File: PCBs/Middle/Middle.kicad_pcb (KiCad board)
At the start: 2 copper layers, 82 x 82 mm, 0 parts

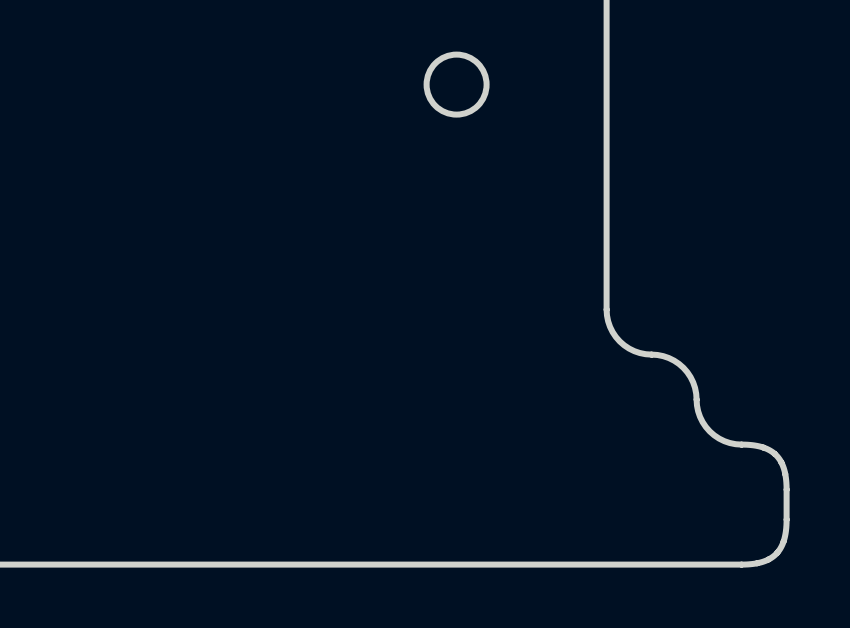
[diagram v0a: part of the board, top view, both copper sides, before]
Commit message: USB-C contact added to mid
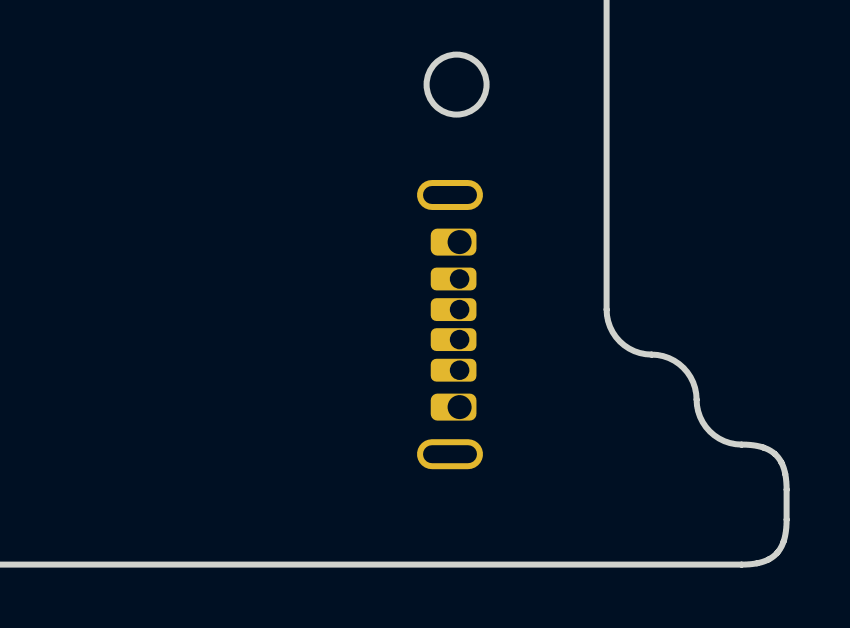
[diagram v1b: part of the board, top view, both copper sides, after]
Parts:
- added J1: USB_C_Receptacle_PowerOnly_6P, Library:TYPE-C-31-D-08, B.Cu at (158.4, 134.0)
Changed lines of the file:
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@@
   )
   (net 0 "")
+  (net 1 "/CC1")
+  (net 2 "+5V")
+  (net 3 "GND")
+  (net 4 "/CC2")
+  (footprint "Library:TYPE-C-31-D-08" (layer "B.Cu")
+    (at 158.45 134 90)
+    (property "Sheetfile" "Middle.kicad_sch")
+    (property "Sheetname" "")
+    (property "ki_description" "USB Power-Only 6P Type-C Receptacle connector")
+    (property "ki_keywords" "usb universal serial bus type-C power-only charging-only 6P 6C")
+    (attr through_hole)
+    (fp_text reference "J1" (at -0.1 4.75 270 unlocked) (layer "B.SilkS")
+        (effects (font (size 1 1) (thickness 0.15)) (justify mirror))
+    )
+    (fp_text value "USB_C_Receptacle_PowerOnly_6P" (at -0.1 -1.45 270 unlocked) (layer "B.Fab")
+        (effects (font (size 1 1) (thickness 0.15)) (justify mirror))
+    )
+    (fp_text user "${REFERENCE}" (at -0.2 -2.95 270 unlocked) (layer "B.Fab")
+        (effects (font (size 1 1) (thickness 0.15)) (justify mirror))
+    )
+    (fp_line (start -4.47 1.3) (end -4.47 1.86)
+      (stroke (width 0.1) (type default)) (layer "B.SilkS"))
+    (fp_line (start -3.17 3.16) (end 3.17 3.16)
+      (stroke (width 0.1) (type default)) (layer "B.SilkS"))
+    (fp_line (start 3.17 0) (end -3.17 0)
+      (stroke (width 0.1) (type default)) (layer "B.SilkS"))
+    (fp_line (start 4.47 1.86) (end 4.47 1.3)
+      (stroke (width 0.1) (type default)) (layer "B.SilkS"))
+    (fp_arc (start -4.47 1.3) (mid -4.089239 0.380761) (end -3.17 0)
+      (stroke (width 0.1) (type default)) (layer "B.SilkS"))
+    (fp_arc (start -3.17 3.16) (mid -4.089239 2.779239) (end -4.47 1.86)
+      (stroke (width 0.1) (type default)) (layer "B.SilkS"))
+    (fp_arc (start 3.17 0) (mid 4.089239 0.380761) (end 4.47 1.3)
+      (stroke (width 0.1) (type default)) (layer "B.SilkS"))
+    (fp_arc (start 4.47 1.86) (mid 4.089239 2.779239) (end 3.17 3.16)
+      (stroke (width 0.1) (type default)) (layer "B.SilkS"))
+    (pad "A5" thru_hole roundrect (at -0.5 1.65 90) (size 0.762 1.524) (drill 0.65 (offset 0 -0.2)) (layers "*.Cu" "*.Mask") (roundrect_rratio 0.25)
+      (net 1 "/CC1") (pinfunction "CC1") (pintype "bidirectional"))
+    (pad "A9" thru_hole roundrect (at 1.52 1.65 90) (size 0.762 1.524) (drill 0.65 (offset 0 -0.2)) (layers "*.Cu" "*.Mask") (roundrect_rratio 0.25)
+      (net 2 "+5V") (pinfunction "VBUS") (pintype "passive"))
+    (pad "A12" thru_hole roundrect (at 2.75 1.65 90) (size 0.9 1.524) (drill 0.8 (offset 0 -0.2)) (layers "*.Cu" "*.Mask") (roundrect_rratio 0.25)
+      (net 3 "GND") (pinfunction "GND") (pintype "passive"))
+    (pad "B5" thru_hole roundrect (at 0.5 1.65 90) (size 0.762 1.524) (drill 0.65 (offset 0 -0.2)) (layers "*.Cu" "*.Mask") (roundrect_rratio 0.25)
+      (net 4 "/CC2") (pinfunction "CC2") (pintype "bidirectional"))
+    (pad "B9" thru_hole roundrect (at -1.52 1.65 90) (size 0.762 1.524) (drill 0.65 (offset 0 -0.2)) (layers "*.Cu" "*.Mask") (roundrect_rratio 0.25)
+      (net 2 "+5V") (pinfunction "VBUS") (pintype "passive"))
+    (pad "B12" thru_hole roundrect (at -2.75 1.65 90) (size 0.9 1.524) (drill 0.8 (offset 0 -0.2)) (layers "*.Cu" "*.Mask") (roundrect_rratio 0.25)
+      (net 3 "GND") (pinfunction "GND") (pintype "passive"))
+    (pad "S1" thru_hole oval (at -4.32 1.33 90) (size 1 2.2) (drill oval 0.6 1.8) (layers "*.Cu" "*.Mask")
+      (net 3 "GND") (pinfunction "SHIELD") (pintype "passive"))
+    (pad "S1" thru_hole oval (at 4.32 1.33 90) (size 1 2.2) (drill oval 0.6 1.8) (layers "*.Cu" "*.Mask")
+      (net 3 "GND") (pinfunction "SHIELD") (pintype "passive"))
+    (model "${KIPRJMOD}/Library.pretty/footprint_test-v2.step"
+      (offset (xyz -15.8 -5.56 0))
+      (scale (xyz 1 1 1))
+      (rotate (xyz -90 0 -90))
+    )
+  )
   (gr_line locked (start 161.7 131.1) (end 161.7 136.9)
     (stroke (width 0.2) (type solid)) (layer "Cmts.User"))

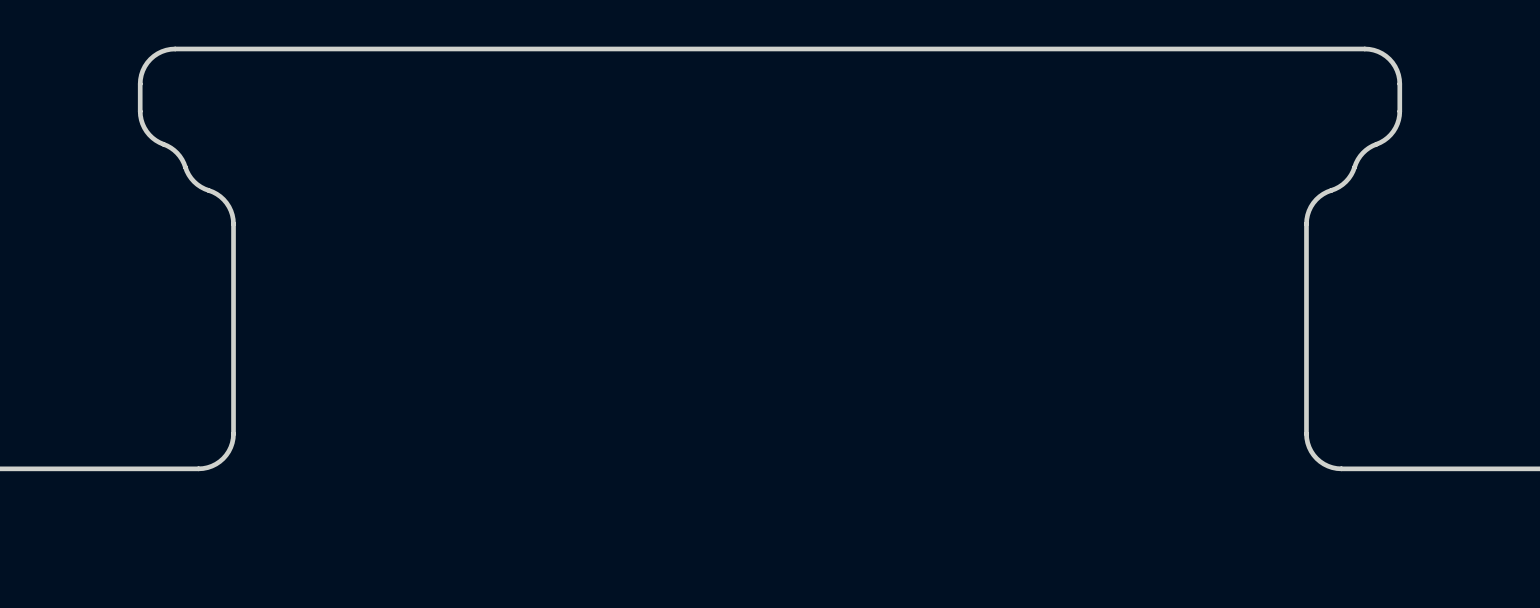
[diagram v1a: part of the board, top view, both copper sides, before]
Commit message: Middle silks
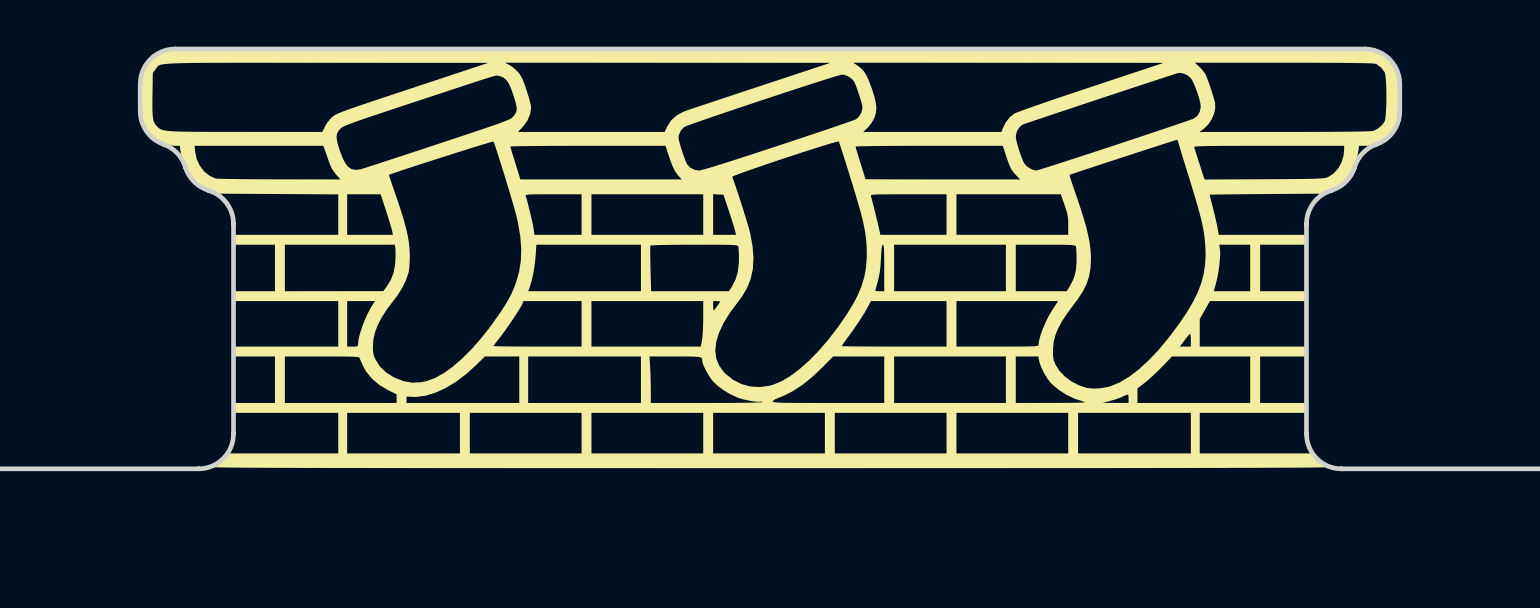
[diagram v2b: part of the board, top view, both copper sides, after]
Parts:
- added G***: LOGO, LOGO, F.Cu at (130.0, 101.0)

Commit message: Middle pcb done
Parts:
- added J2: PWR, Connector_PinHeader_2.54mm:PinHeader_1x04_P2.54mm_Vertical, F.Cu at (100.0, 106.2)
- added J3: CAP_TOUCH, Connector_PinHeader_2.54mm:PinHeader_1x04_P2.54mm_Vertical, F.Cu at (160.0, 106.2)
- added TP1: TOUCH1, Library:CapPad, F.Cu at (116.0, 68.0)
- added TP2: TOUCH2, Library:CapPad, F.Cu at (131.0, 68.0)
- added TP3: TOUCH3, Library:CapPad, F.Cu at (145.0, 68.0)
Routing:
- net /TOUCH3: track 0.00 -> 80.1 mm
- net /TOUCH2: track 0.00 -> 65.3 mm
- net /TOUCH1: track 0.00 -> 47.3 mm
- net /CC1: track 0.00 -> 28.0 mm
- net /CC2: track 0.00 -> 23.3 mm
- added copper zone on F.Cu, net +5V
- added copper zone on B.Cu, net GND

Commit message: fixed step files
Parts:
- TP1, TP2, TP3: footprint Library:CapPad -> cap_sock:cap_sock
- moved TP3 0.92 mm to (145.6, 67.3)
- moved TP1 0.87 mm to (116.5, 67.2)
- moved TP2 0.68 mm to (131.2, 67.3)
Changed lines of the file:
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@@
     )
     (pad_to_mask_clearance 0)
+    (aux_axis_origin 129.65 140.65)
     (pcbplotparams
       (layerselection 0x00010fc_ffffffff)
@@
       (net 4 "/CC2") (pinfunction "Pin_4") (pintype "passive"))
   )
-  (footprint "Library:CapPad" (layer "F.Cu")
-    (at 116 68)
+  (footprint "cap_sock:cap_sock" (layer "F.Cu")
+    (at 145.635654 67.331541)
     (property "Sheetfile" "Middle.kicad_sch")
     (property "Sheetname" "")
@@
     (property "ki_keywords" "test point tp")
     (attr smd)
-    (fp_text reference "TP1" (at 3.9 5.7 unlocked) (layer "F.SilkS") hide
+    (fp_text reference "TP3" (at 0 -0.5 unlocked) (layer "F.SilkS") hide
         (effects (font (size 1 1) (thickness 0.1)))
     )
-    (fp_text value "TOUCH1" (at 0 1 unlocked) (layer "F.Fab")
+    (fp_text value "TOUCH3" (at 0 1 unlocked) (layer "F.Fab") hide
         (effects (font (size 1 1) (thickness 0.15)))
     )
-    (fp_text user "${REFERENCE}" (at 0 2.5 unlocked) (layer "F.Fab")
-        (effects (font (size 1 1) (thickness 0.15)))
-    )
-    (pad "1" smd circle (at 0 0) (size 10 10) (layers "F.Cu" "F.Paste")
-      (net 5 "/TOUCH1") (pinfunction "1") (pintype "passive"))
+    (pad "1" smd custom (at 0 3.6) (size 2.286 2.286) (layers "F.Cu" "F.Paste")
+      (net 7 "/TOUCH3") (pinfunction "1") (pintype "passive") (thermal_bridge_angle 45)
+      (options (clearance outline) (anchor circle))
+      (primitives
+        (gr_poly
+          (pts
+            (xy -0.986112 3.603613)
+            (xy -1.618959 3.715068)
+            (xy -2.244652 3.638361)
+            (xy -2.862502 3.363651)
+            (xy -3.579301 2.646845)
+            (xy -3.774587 1.744484)
+            (xy -3.476669 0.709748)
+            (xy -2.71386 -0.404179)
+            (xy -2.373613 -0.928337)
+            (xy -2.2 -1.5)
+            (xy -2.244174 -2.761999)
+            (xy -2.629385 -4.142486)
+            (xy -3.138633 -5.593772)
+            (xy -3.162998 -5.66752)
+            (xy -3.855271 -5.438806)
+            (xy -4.554394 -5.486939)
+            (xy -5.014261 -6.008841)
+            (xy -5.273489 -6.773012)
+            (xy -5.224716 -7.46296)
+            (xy -4.695874 -7.916791)
+            (xy 1.543446 -9.978149)
+            (xy 2.242569 -9.930015)
+            (xy 2.702436 -9.408113)
+            (xy 2.961664 -8.643942)
+            (xy 2.912891 -7.953995)
+            (xy 2.384049 -7.500164)
+            (xy 1.903638 -7.341445)
+            (xy 1.979217 -7.112682)
+            (xy 2.702758 -4.787184)
+            (xy 3.154785 -2.905386)
+            (xy 3.202182 -2.049534)
+            (xy 3.089543 -1.207)
+            (xy 2.786147 -0.345246)
+            (xy 2.261276 0.568264)
+            (xy 0.94845 2.238662)
+            (xy -0.346802 3.313834)
+          )
+          (width 0.2) (fill yes))
+      ))
   )
-  (footprint "Library:CapPad" (layer "F.Cu")
-    (at 131 68)
+  (footprint "cap_sock:cap_sock" (layer "F.Cu")
+    (at 116.45 67.25)
     (property "Sheetfile" "Middle.kicad_sch")
     (property "Sheetname" "")
@@
     (property "ki_keywords" "test point tp")
     (attr smd)
-    (fp_text reference "TP2" (at 3.9 5.7 unlocked) (layer "F.SilkS") hide
+    (fp_text reference "TP1" (at 0 -0.5 unlocked) (layer "F.SilkS") hide
         (effects (font (size 1 1) (thickness 0.1)))
     )
-    (fp_text value "TOUCH2" (at 0 1 unlocked) (layer "F.Fab")
+    (fp_text value "TOUCH1" (at 0 1 unlocked) (layer "F.Fab") hide
         (effects (font (size 1 1) (thickness 0.15)))
     )
-    (fp_text user "${REFERENCE}" (at 0 2.5 unlocked) (layer "F.Fab")
-        (effects (font (size 1 1) (thickness 0.15)))
-    )
-    (pad "1" smd circle (at 0 0) (size 10 10) (layers "F.Cu" "F.Paste")
-      (net 6 "/TOUCH2") (pinfunction "1") (pintype "passive"))
+    (pad "1" smd custom (at 0 3.6) (size 2.286 2.286) (layers "F.Cu" "F.Paste")
+      (net 5 "/TOUCH1") (pinfunction "1") (pintype "passive") (thermal_bridge_angle 45)
+      (options (clearance outline) (anchor circle))
+      (primitives
+        (gr_poly
+          (pts
+            (xy -0.986112 3.603613)
+            (xy -1.618959 3.715068)
+            (xy -2.244652 3.638361)
+            (xy -2.862502 3.363651)
+            (xy -3.579301 2.646845)
+            (xy -3.774587 1.744484)
+            (xy -3.476669 0.709748)
+            (xy -2.71386 -0.404179)
+            (xy -2.373613 -0.928337)
+            (xy -2.2 -1.5)
+            (xy -2.244174 -2.761999)
+            (xy -2.629385 -4.142486)
+            (xy -3.138633 -5.593772)
+            (xy -3.162998 -5.66752)
+            (xy -3.855271 -5.438806)
+            (xy -4.554394 -5.486939)
+            (xy -5.014261 -6.008841)
+            (xy -5.273489 -6.773012)
+            (xy -5.224716 -7.46296)
+            (xy -4.695874 -7.916791)
+            (xy 1.543446 -9.978149)
+            (xy 2.242569 -9.930015)
+            (xy 2.702436 -9.408113)
+            (xy 2.961664 -8.643942)
+            (xy 2.912891 -7.953995)
+            (xy 2.384049 -7.500164)
+            (xy 1.903638 -7.341445)
+            (xy 1.979217 -7.112682)
+            (xy 2.702758 -4.787184)
+            (xy 3.154785 -2.905386)
+            (xy 3.202182 -2.049534)
+            (xy 3.089543 -1.207)
+            (xy 2.786147 -0.345246)
+            (xy 2.261276 0.568264)
+            (xy 0.94845 2.238662)
+            (xy -0.346802 3.313834)
+          )
+          (width 0.2) (fill yes))
+      ))
   )
   (footprint "LOGO" (layer "F.Cu")
@@
       (stroke (width 0) (type solid)) (fill solid) (layer "F.SilkS"))
   )
-  (footprint "Library:CapPad" (layer "F.Cu")
-    (at 145 68)
-    (property "Sheetfile" "Middle.kicad_sch")
-    (property "Sheetname" "")
-    (property "ki_description" "test point")
-    (property "ki_keywords" "test point tp")
-    (attr smd)
-    (fp_text reference "TP3" (at 3.9 5.7 unlocked) (layer "F.SilkS") hide
-        (effects (font (size 1 1) (thickness 0.1)))
-    )
-    (fp_text value "TOUCH3" (at 0 1 unlocked) (layer "F.Fab")
-        (effects (font (size 1 1) (thickness 0.15)))
-    )
-    (fp_text user "${REFERENCE}" (at 0 2.5 unlocked) (layer "F.Fab")
-        (effects (font (size 1 1) (thickness 0.15)))
-    )
-    (pad "1" smd circle (at 0 0) (size 10 10) (layers "F.Cu" "F.Paste")
-      (net 7 "/TOUCH3") (pinfunction "1") (pintype "passive"))
-  )
   (footprint "Connector_PinHeader_2.54mm:PinHeader_1x04_P2.54mm_Vertical" (layer "F.Cu")
     (at 100 106.2)
@@
       (net 3 "GND") (pinfunction "Pin_4") (pintype "passive"))
   )
+  (footprint "cap_sock:cap_sock" (layer "F.Cu")
+    (at 131.2 67.35)
+    (property "Sheetfile" "Middle.kicad_sch")
+    (property "Sheetname" "")
+    (property "ki_description" "test point")
+    (property "ki_keywords" "test point tp")
+    (attr smd)
+    (fp_text reference "TP2" (at 0 -0.5 unlocked) (layer "F.SilkS") hide
+        (effects (font (size 1 1) (thickness 0.1)))
+    )
+    (fp_text value "TOUCH2" (at 0 1 unlocked) (layer "F.Fab") hide
+        (effects (font (size 1 1) (thickness 0.15)))
+    )
+    (pad "1" smd custom (at 0 3.6) (size 2.286 2.286) (layers "F.Cu" "F.Paste")
+      (net 6 "/TOUCH2") (pinfunction "1") (pintype "passive") (thermal_bridge_angle 45)
+      (options (clearance outline) (anchor circle))
+      (primitives
+        (gr_poly
+          (pts
+            (xy -0.986112 3.603613)
+            (xy -1.618959 3.715068)
+            (xy -2.244652 3.638361)
+            (xy -2.862502 3.363651)
+            (xy -3.579301 2.646845)
+            (xy -3.774587 1.744484)
+            (xy -3.476669 0.709748)
+            (xy -2.71386 -0.404179)
+            (xy -2.373613 -0.928337)
+            (xy -2.2 -1.5)
+            (xy -2.244174 -2.761999)
+            (xy -2.629385 -4.142486)
+            (xy -3.138633 -5.593772)
+            (xy -3.162998 -5.66752)
+            (xy -3.855271 -5.438806)
+            (xy -4.554394 -5.486939)
+            (xy -5.014261 -6.008841)
+            (xy -5.273489 -6.773012)
+            (xy -5.224716 -7.46296)
+            (xy -4.695874 -7.916791)
+            (xy 1.543446 -9.978149)
+            (xy 2.242569 -9.930015)
+            (xy 2.702436 -9.408113)
+            (xy 2.961664 -8.643942)
+            (xy 2.912891 -7.953995)
+            (xy 2.384049 -7.500164)
+            (xy 1.903638 -7.341445)
+            (xy 1.979217 -7.112682)
+            (xy 2.702758 -4.787184)
+            (xy 3.154785 -2.905386)
+            (xy 3.202182 -2.049534)
+            (xy 3.089543 -1.207)
+            (xy 2.786147 -0.345246)
+            (xy 2.261276 0.568264)
+            (xy 0.94845 2.238662)
+            (xy -0.346802 3.313834)
+          )
+          (width 0.2) (fill yes))
+      ))
+  )
   (footprint "Library:TYPE-C-31-D-08" (layer "B.Cu")

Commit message: Almost final adjustments
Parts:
- added G***: LOGO, LOGO, F.Cu at (131.8, 68.3)
- added G***: LOGO, LOGO, F.Cu at (146.1, 68.5)
- added G***: LOGO, LOGO, F.Cu at (116.9, 68.2)
- J2: value PWR -> CAPTOUCH
- J3: value CAP_TOUCH -> PWR
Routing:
- net /TOUCH2: track 65.3 -> 64.7 mm
- added copper zone on F.Cu, net GND

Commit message: Adjusted icons
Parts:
- removed the G*** at (131.8, 68.3)
- removed the G*** at (146.1, 68.5)
- removed the G*** at (116.9, 68.2)
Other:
- board text added: "JLCJLCJLCJLC"
